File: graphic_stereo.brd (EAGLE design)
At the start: 109 x 29.5 mm, 82 parts, among them IC1 NE5532D, IC2 NE5532D, IC3 NE5532D, IC4 NE5532D, IC5 NE5532D

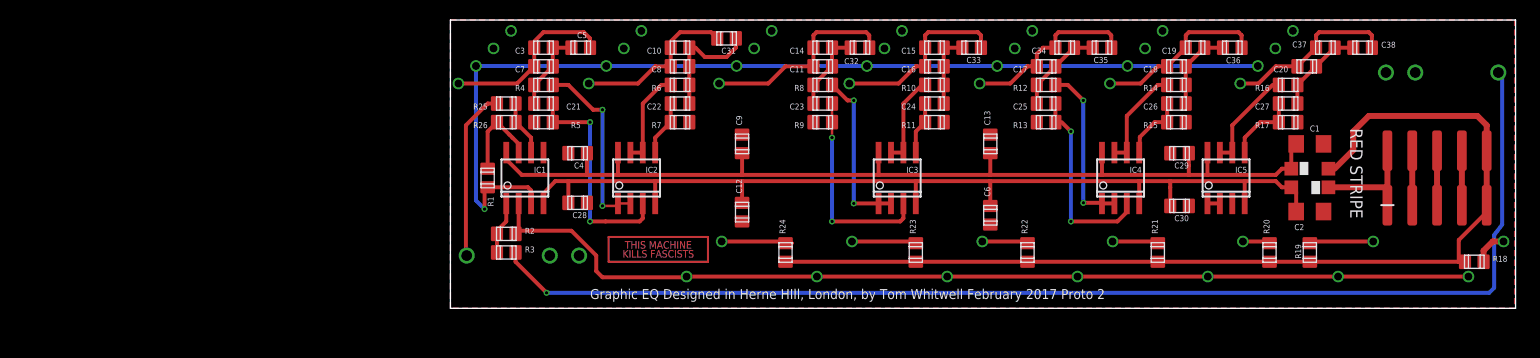
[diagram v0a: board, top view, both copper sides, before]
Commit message: Revert "Merge branch 'fix-panel'"
This reverts commit 24303b16601d2e124062e02205cddf4c546a9bcf, reversing
changes made to eef96a0ff0da711b8061c4b766c52a963260b08f.
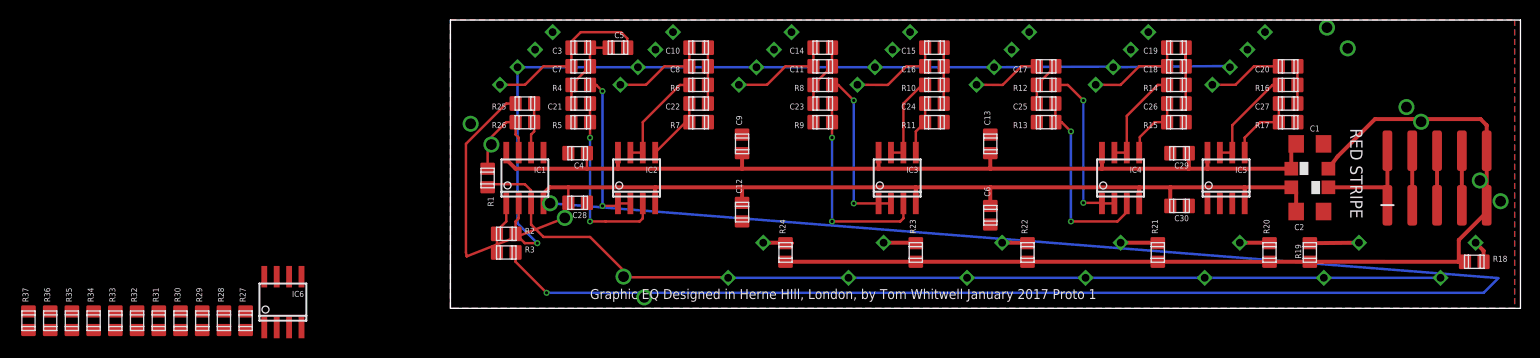
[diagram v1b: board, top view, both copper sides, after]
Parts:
- removed C31, C32, C33, C34, C35, C36, C37, C38: NP, we-rcl:C0805
- removed U$1: (no value), MusicThingModular:TMKF
- added IC6: NE5532D, linear:SO08
- added L_OUT, R_OUT: THONKICONNNEW, MusicThingModular:WQP-PJ301M-12_JACK
- added R27, R28: 470R, we-rcl:C0805
- added R29, R30, R31, R32, R33, R34, R35, R36, R37: 2.7k, we-rcl:C0805
- 160HZ, 16KHZ, 1KHZ, 2.5KHZ, 410HZ, 63HZ, 7.7KHZ: device MusicThingModular:ALPHA_ILL_FADER_20MM_REV2 -> TomW:ALPHA_ILL_FADER_20MM
- R18, R19, R20, R21, R22, R23, R24: value 2k -> 470R
- moved OUTPUT 96.1 mm to (6.67, 14.3), turned to 135 degrees
- moved INPUT 8.58 mm to (15.2, 5.71), turned to 315 degrees
- moved 63HZ 4.26 mm to (18.5, 14.8)
- moved C21 3.81 mm to (13.3, 21.0)
- moved C3 3.81 mm to (13.3, 26.7)
- moved C7 3.81 mm to (13.3, 24.8)
- moved R4 3.81 mm to (13.3, 22.9)
- moved R5 3.81 mm to (13.3, 19.1)
- moved C5 3.81 mm to (17.1, 26.7)
- moved 160HZ 3.24 mm to (30.9, 14.8)
- moved 16KHZ 2.86 mm to (91.4, 14.8)
- moved 410HZ 2.04 mm to (43.0, 14.8)
- moved C19 1.91 mm to (74.3, 26.7)
- moved C20 1.91 mm to (85.7, 24.8)
- moved R25 1.91 mm to (7.62, 21.0)
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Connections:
- new net N$1: IC6.1, R27.2, R29.1
- new net N$44: R28.1, R_OUT.P$1_TIP
- new net N$46: IC6.7, R28.2, R30.1
- new net N$47: IC6.6, R30.2, R32.2, R34.2, R36.2
- new net N$49: IC6.2, R29.2, R31.2, R33.2, R35.2, R37.2
- net +12V: now also IC6.8
- net -12V: now also IC6.4
- net GND: now also IC6.3, IC6.5, L_OUT.P$3_SLEEVE, R_OUT.P$3_SLEEVE; no longer IC5.3
- net N$11: no longer C34.1, C35.2
- net N$12: no longer C33.2
- net N$14: no longer C31.1
- net N$18: no longer C31.2
- net N$19: no longer C36.1
- net N$21: now also R33.1
- net N$22: now also L_OUT.P$1_TIP, R27.1; no longer IC5.1, IC5.2
- net N$23: no longer C37.1, C38.1
- net N$26: now also R31.1
- net N$27: now also R34.1
- net N$29: now also R32.1
- net N$3: now also IC1.3, R1.1; no longer IC1.2, R2.1
- net N$30: no longer C32.1
- net N$31: no longer C33.1
- net N$33: now also R35.1
- net N$35: now also R36.1
- net N$36: no longer C34.2, C35.1
- net N$37: no longer C36.2
- net N$39: now also R37.1
- net N$4: no longer C32.2
- net N$40: no longer C37.2, C38.2
- net N$7: now also IC1.2, R2.1; no longer IC1.3, R1.1
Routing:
- net N$6: track 125.1 -> 200.8 mm
- net N$11: track 18.5 -> 6.96 mm
- net N$2: track 17.6 -> 29.1 mm
- net N$4: track 20.8 -> 10.3 mm
- net N$23: track 17.8 -> 7.59 mm
- net N$12: track 18.9 -> 9.63 mm
- net N$19: track 17.8 -> 10.0 mm
- net N$14: track 17.1 -> 9.75 mm
- net -12V: track 101.0 -> 94.1 mm
- net N$18: track 12.2 -> 5.72 mm
- net +12V: track 103.2 -> 97.6 mm
- net N$7: track 103.3 -> 97.7 mm
- net N$40: track 9.20 -> 3.81 mm
- net N$36: track 9.20 -> 4.60 mm
- net N$25: track 22.9 -> 19.1 mm
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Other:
- board size 109 x 29.5 mm -> 109.5 x 29.5 mm
- board text added: "Graphic EQ Designed in Herne HIll, London, by Tom Whitwell January 2017 Proto 1"
- board text removed: "Graphic EQ Designed in Herne HIll, London, by Tom Whitwell February 2017 Proto 2"
